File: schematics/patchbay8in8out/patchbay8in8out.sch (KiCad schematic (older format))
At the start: 13 parts

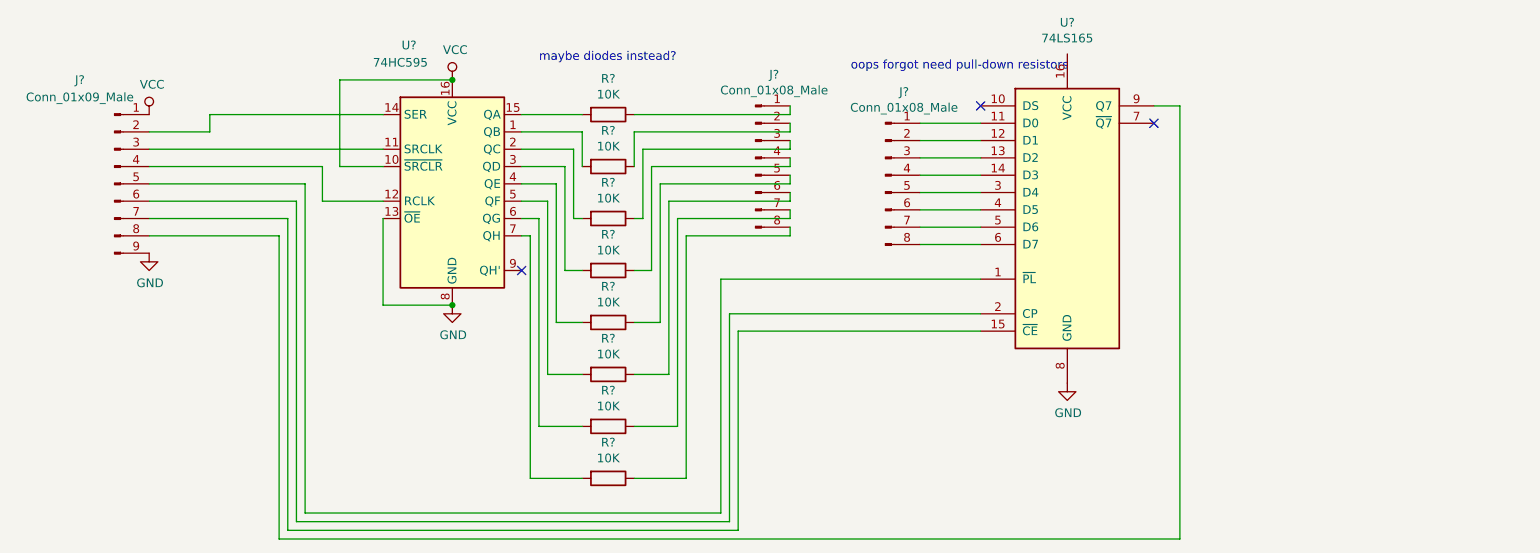
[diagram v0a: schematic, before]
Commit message: updated patchbay schematic with diodes and pulldown resistors
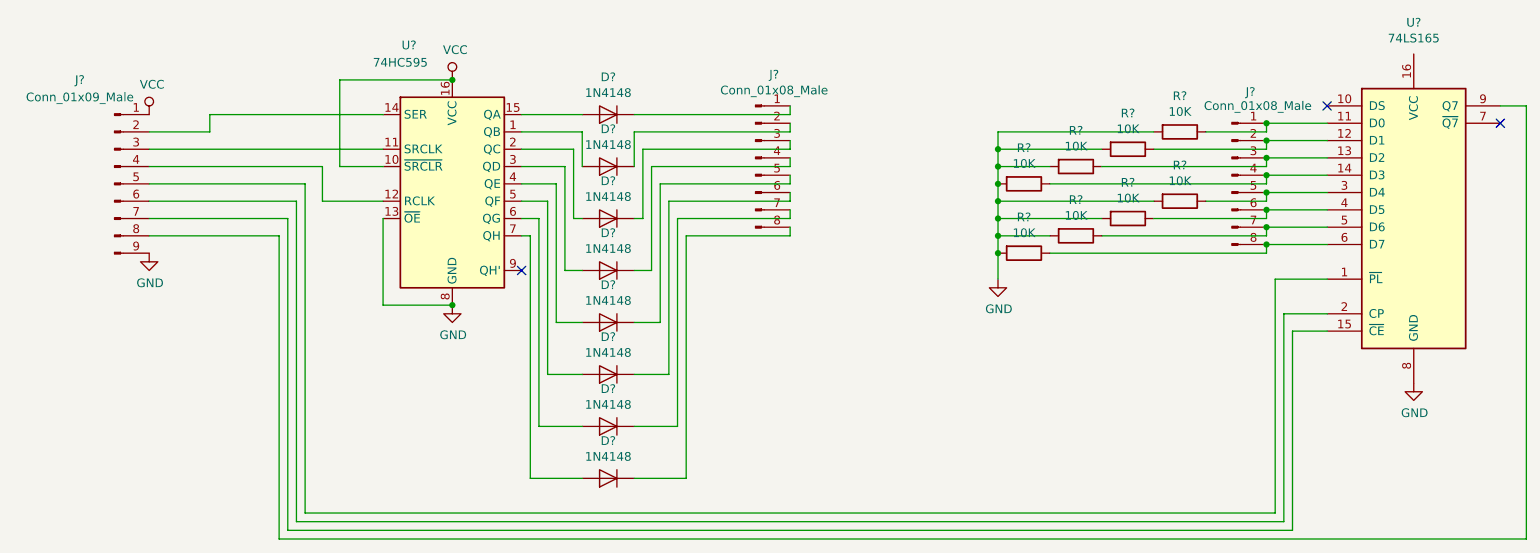
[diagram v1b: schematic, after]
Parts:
- removed R? (x4): 10K, symbol Device:R
- added D? (x8): 1N4148, Diode_THT:D_DO-35_SOD27_P7.62mm_Horizontal, symbol Diode:1N4148
- added R? (x4): 10K, symbol Device:R
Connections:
- net GND: now also R?.2, R?.2, R?.2, R?.2, R?.2, R?.2, R?.2, R?.2
- net at U?.1 (QB): now also D?.2 (A); no longer R?.2
- net at U?.15 (QA): now also D?.2 (A); no longer R?.2
- net at U?.2 (QC): now also D?.2 (A); no longer R?.2
- net at U?.3 (QD): now also D?.2 (A); no longer R?.2
- net at U?.4 (QE): now also D?.2 (A)
- net at U?.5 (QF): now also D?.2 (A)
- net at U?.6 (QG): now also D?.2 (A)
- net at U?.7 (QH): now also D?.2 (A)
- net at J?.1 (Pin_1), U?.11 (D0): now also R?.1
- net at J?.2 (Pin_2), U?.12 (D1): now also R?.1
- net at J?.3 (Pin_3), U?.13 (D2): now also R?.1
- net at J?.4 (Pin_4), U?.14 (D3): now also R?.1
- net at J?.5 (Pin_5), U?.3 (D4): now also R?.1
- net at J?.6 (Pin_6), U?.4 (D5): now also R?.1
- net at J?.7 (Pin_7), U?.5 (D6): now also R?.1
- net at J?.8 (Pin_8), U?.6 (D7): now also R?.1
- net at J?.1 (Pin_1): now also D?.1 (K); no longer R?.1
- net at J?.2 (Pin_2): now also D?.1 (K); no longer R?.1
- net at J?.3 (Pin_3): now also D?.1 (K); no longer R?.1
- net at J?.4 (Pin_4): now also D?.1 (K); no longer R?.1
- net at J?.5 (Pin_5): now also D?.1 (K)
- net at J?.6 (Pin_6): now also D?.1 (K)
- net at J?.7 (Pin_7): now also D?.1 (K)
- net at J?.8 (Pin_8): now also D?.1 (K)
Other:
- note removed: "maybe diodes instead?"
- note removed: "oops forgot need pull-down resistors"
- moved on the sheet: J?, R?, U?
